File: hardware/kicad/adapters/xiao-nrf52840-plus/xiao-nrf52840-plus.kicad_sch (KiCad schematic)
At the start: 0 parts

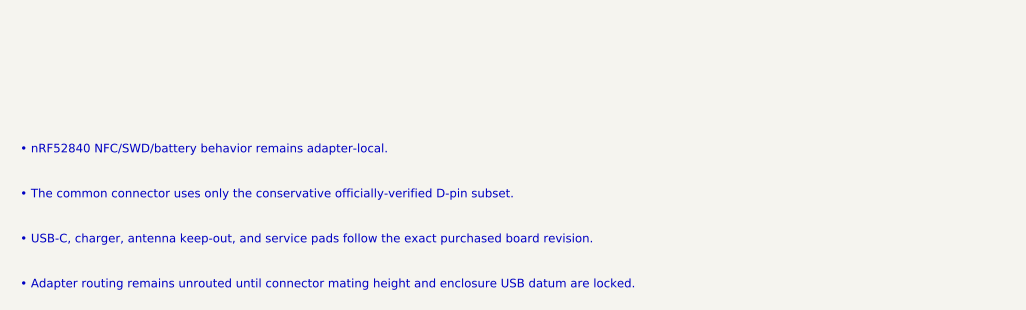
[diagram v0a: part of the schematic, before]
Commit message: Establish a host-verified V1 baseline before physical bring-up
Constraint: The common PCB remains 100 mm square, all controls stay PCB-mounted, and no display is added.
Rejected: Deterministic adapter autorouting | KiCad exposed real escape and via conflicts, so reviewed manual routing remains explicit.
Confidence: medium
Scope-risk: broad
Directive: Do not order boards until all open connections are routed, complete schematics pass parity, exact parts pass sample fit, and physical power/RF/USB/BLE tests succeed.
Tested: KiCad block ERC 0 on three projects; DRC 0 errors with documented warnings and open nets; Blender manifold STL generation; firmware 12/12 normal, sanitized, and embedded-style builds; bridge 41/41 on Python 3.11 and 3.14.
Not-tested: Physical XIAO USB/BLE, RF, battery charging and swelling, touch sensitivity, connector mating, real audio backend, and assembled endurance.
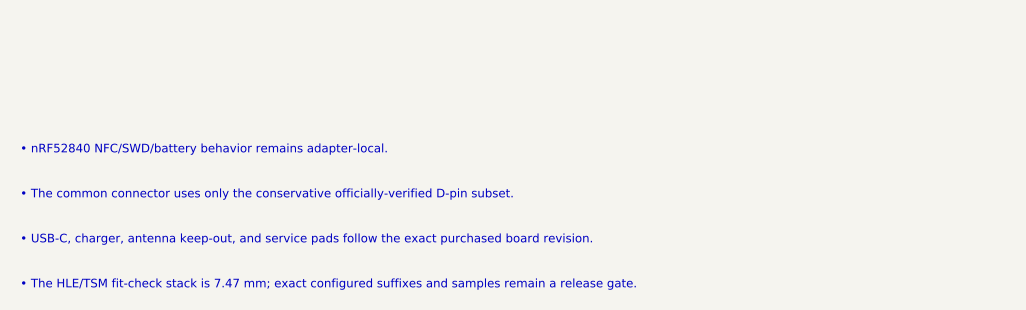
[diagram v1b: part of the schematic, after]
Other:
- note added: "• The HLE/TSM fit-check stack is 7.47 mm; exact configured suffixes and samples remain a release gate."
- note removed: "• Adapter routing remains unrouted until connector mating height and enclosure USB datum are locked."
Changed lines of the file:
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@@
 		)
 	)
-	(text "• Adapter routing remains unrouted until connector mating height and enclosure USB datum are locked."
+	(text "• The HLE/TSM fit-check stack is 7.47 mm; exact configured suffixes and samples remain a release gate."
 		(exclude_from_sim no)
 		(at 18.000 172.000 0)
